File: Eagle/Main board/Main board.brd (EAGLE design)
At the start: 160 x 160 mm, 140 parts, among them IC1 LMZ14202TZE-ADJ_NOPB, IC2 VNH7070ASTR, IC3 VNH7070ASTR, IC4 VNH7070ASTR, IC5 VNH7070ASTR, IC6 ATMEGA32U4-AU, J2 43650-0201, J3 43650-0201, J4 43650-0201, J5 43650-0201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

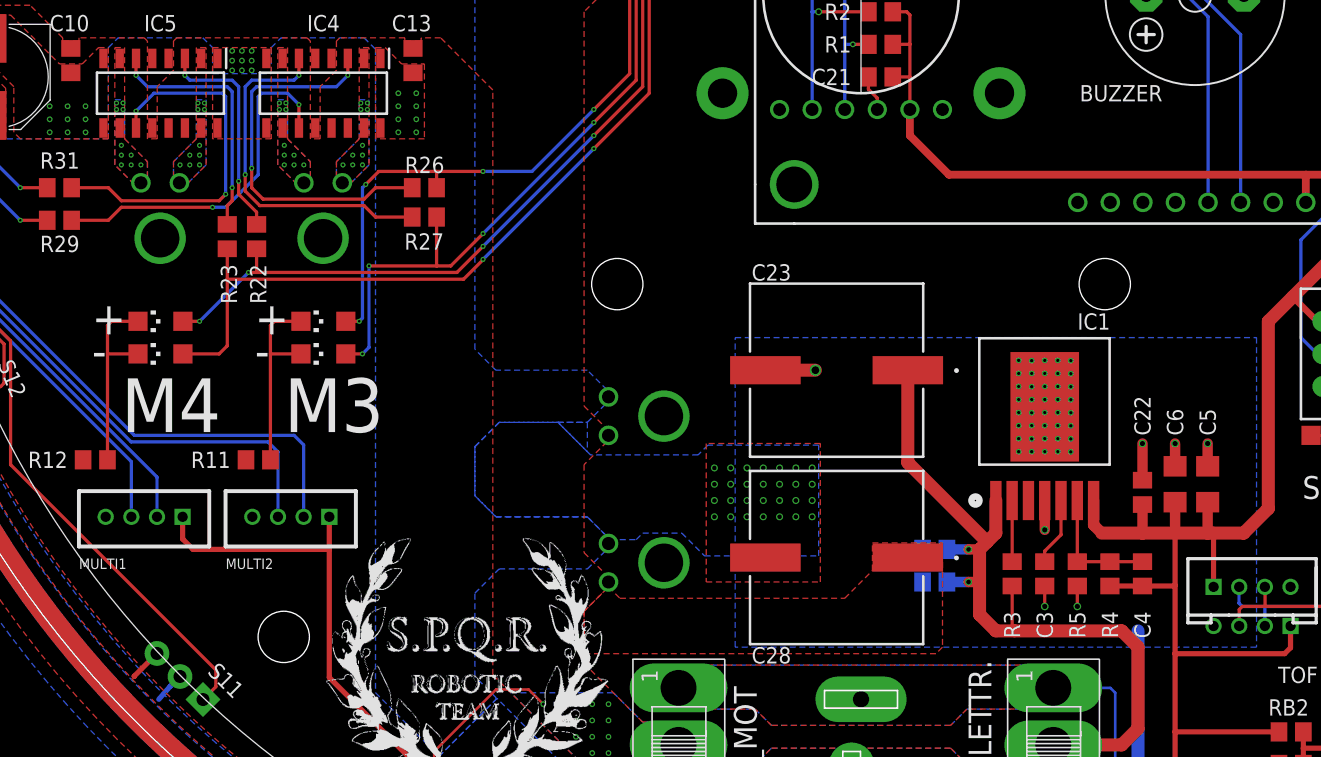
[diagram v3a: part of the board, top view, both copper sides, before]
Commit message: Added JLC's order number place, cleaned files
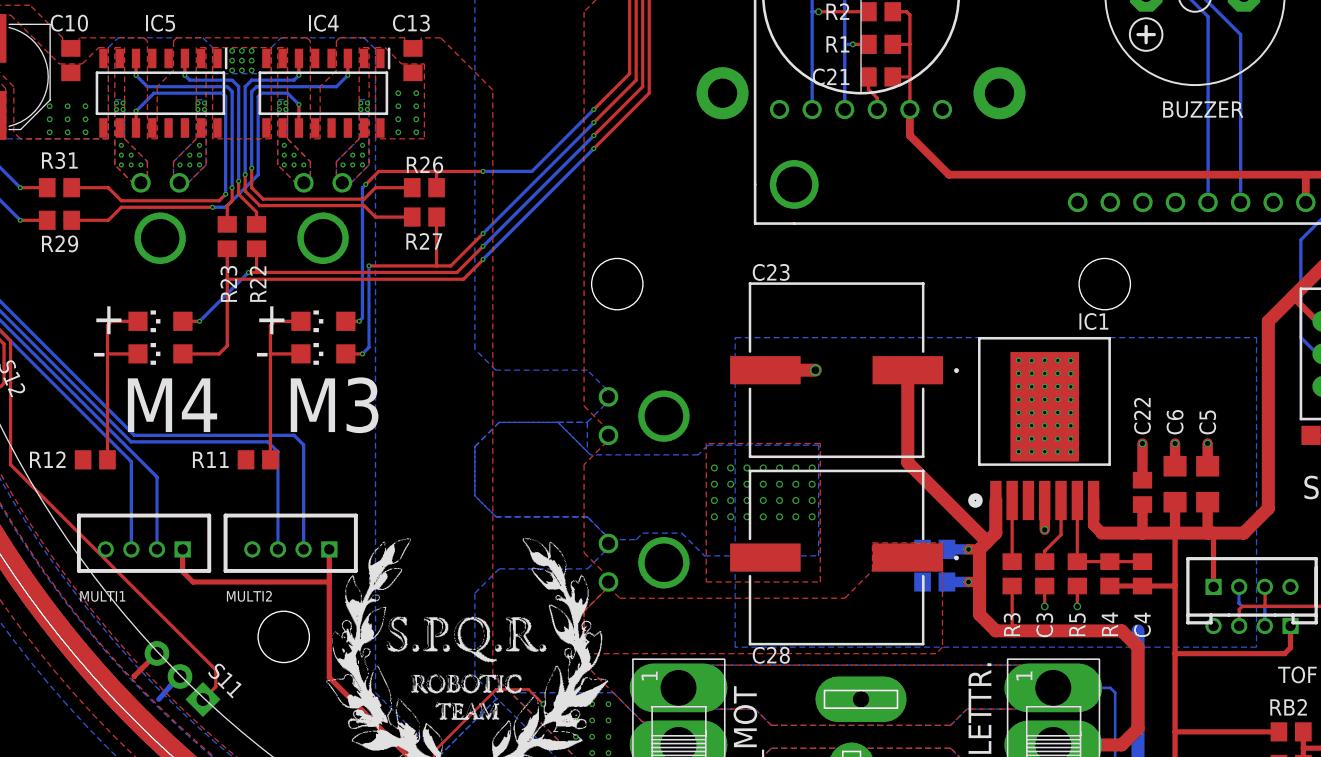
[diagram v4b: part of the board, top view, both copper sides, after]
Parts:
- moved MULTI1 2.54 mm to (-44.5, -43.2)
- moved MULTI2 2.54 mm to (-55.9, -43.2)
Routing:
- net +3V3: track 636.0 -> 633.5 mm
- net MULTI_DIG2: track 180.8 -> 183.4 mm
- net MULTI_DIG1: track 183.8 -> 186.3 mm
- net MULTI_PWM2: track 177.4 -> 179.9 mm
- net MULTI_PWM1: track 181.3 -> 183.9 mm
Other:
- board text added: "JLCJLCJLCJLC"
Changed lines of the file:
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@@
 <layer number="19" name="Unrouted" color="6" fill="1" visible="yes" active="yes"/>
 <layer number="20" name="Dimension" color="24" fill="1" visible="yes" active="yes"/>
-<layer number="21" name="tPlace" color="7" fill="1" visible="yes" active="yes"/>
+<layer number="21" name="tPlace" color="7" fill="1" visible="no" active="yes"/>
 <layer number="22" name="bPlace" color="7" fill="1" visible="yes" active="yes"/>
-<layer number="23" name="tOrigins" color="15" fill="1" visible="yes" active="yes"/>
+<layer number="23" name="tOrigins" color="15" fill="1" visible="no" active="yes"/>
 <layer number="24" name="bOrigins" color="15" fill="1" visible="yes" active="yes"/>
 <layer number="25" name="tNames" color="7" fill="1" visible="yes" active="yes"/>
@@
 <layer number="37" name="tTest" color="7" fill="1" visible="no" active="yes"/>
 <layer number="38" name="bTest" color="7" fill="1" visible="no" active="yes"/>
-<layer number="39" name="tKeepout" color="4" fill="11" visible="yes" active="yes"/>
+<layer number="39" name="tKeepout" color="4" fill="11" visible="no" active="yes"/>
 <layer number="40" name="bKeepout" color="1" fill="11" visible="yes" active="yes"/>
-<layer number="41" name="tRestrict" color="4" fill="10" visible="yes" active="yes"/>
+<layer number="41" name="tRestrict" color="4" fill="10" visible="no" active="yes"/>
 <layer number="42" name="bRestrict" color="1" fill="10" visible="yes" active="yes"/>
 <layer number="43" name="vRestrict" color="2" fill="10" visible="no" active="yes"/>
@@
 <layer number="49" name="Reference" color="7" fill="1" visible="no" active="yes"/>
 <layer number="50" name="dxf" color="7" fill="1" visible="no" active="no"/>
-<layer number="51" name="tDocu" color="7" fill="1" visible="yes" active="yes"/>
+<layer number="51" name="tDocu" color="7" fill="1" visible="no" active="yes"/>
 <layer number="52" name="bDocu" color="7" fill="1" visible="yes" active="yes"/>
 <layer number="53" name="tGND_GNDA" color="7" fill="1" visible="no" active="no"/>
@@
 <text x="49.53" y="23.368" size="0.8128" layer="25">PALLA_PRESA</text>
 <text x="56.642" y="23.368" size="0.8128" layer="26" rot="MR0">PALLA_PRESA</text>
-<wire x1="-60.966" y1="-38.636" x2="-50.806" y2="-38.636" width="0.3048" layer="25"/>
-<wire x1="-50.806" y1="-38.636" x2="-50.806" y2="-42.954" width="0.3048" layer="25"/>
-<wire x1="-50.806" y1="-42.954" x2="-60.966" y2="-42.954" width="0.3048" layer="25"/>
-<wire x1="-60.966" y1="-42.954" x2="-60.966" y2="-38.636" width="0.3048" layer="25"/>
-<wire x1="-49.536" y1="-38.636" x2="-39.376" y2="-38.636" width="0.3048" layer="25"/>
-<wire x1="-39.376" y1="-38.636" x2="-39.376" y2="-42.954" width="0.3048" layer="25"/>
-<wire x1="-39.376" y1="-42.954" x2="-49.536" y2="-42.954" width="0.3048" layer="25"/>
-<wire x1="-49.536" y1="-42.954" x2="-49.536" y2="-38.636" width="0.3048" layer="25"/>
-<text x="-60.96" y="-44.704" size="0.8128" layer="25">MULTI1</text>
-<text x="-49.53" y="-44.704" size="0.8128" layer="25">MULTI2</text>
+<wire x1="-60.966" y1="-40.541" x2="-50.806" y2="-40.541" width="0.3048" layer="25"/>
+<wire x1="-50.806" y1="-40.541" x2="-50.806" y2="-44.859" width="0.3048" layer="25"/>
+<wire x1="-50.806" y1="-44.859" x2="-60.966" y2="-44.859" width="0.3048" layer="25"/>
+<wire x1="-60.966" y1="-44.859" x2="-60.966" y2="-40.541" width="0.3048" layer="25"/>
+<wire x1="-49.536" y1="-40.541" x2="-39.376" y2="-40.541" width="0.3048" layer="25"/>
+<wire x1="-39.376" y1="-40.541" x2="-39.376" y2="-44.859" width="0.3048" layer="25"/>
+<wire x1="-39.376" y1="-44.859" x2="-49.536" y2="-44.859" width="0.3048" layer="25"/>
+<wire x1="-49.536" y1="-44.859" x2="-49.536" y2="-40.541" width="0.3048" layer="25"/>
+<text x="-60.96" y="-47.244" size="0.8128" layer="25">MULTI1</text>
+<text x="-49.53" y="-47.244" size="0.8128" layer="25">MULTI2</text>
 <rectangle x1="-28.014290625" y1="-61.546103125" x2="-27.719653125" y2="-61.509271875" layer="25"/>
 <rectangle x1="-28.1616125" y1="-61.509271875" x2="-27.682825" y2="-61.472446875" layer="25"/>
@@
 <text x="-33.02" y="31.115" size="1.778" layer="26" rot="MR0">Morco</text>
 <text x="5.08" y="43.18" size="1.27" layer="26" rot="MR0">Designed by Dario Casagrande</text>
+<text x="5.08" y="5.715" size="1.016" layer="26" rot="MR0">JLCJLCJLCJLC</text>
 </plain>
 <attributes>
@@
 <attribute name="MF" value="" x="1.905" y="72.39" size="1.778" layer="27" rot="R180" display="off"/>
 <attribute name="MPN" value="" x="1.905" y="72.39" size="1.778" layer="27" rot="R180" display="off"/>
-<attribute name="NAME" x="23.495" y="-6.985" size="1.27" layer="25" ratio="10" rot="R180"/>
+<attribute name="NAME" x="29.845" y="-8.255" size="1.27" layer="25" ratio="10" rot="R180"/>
 <attribute name="OC_FARNELL" value="unknown" x="1.905" y="72.39" size="1.778" layer="27" rot="R180" display="off"/>
 <attribute name="OC_NEWARK" value="unknown" x="1.905" y="72.39" size="1.778" layer="27" rot="R180" display="off"/>
@@
 <attribute name="VALUE" x="5.715" y="41.275" size="1.27" layer="27" rot="R180"/>
 </element>
-<element name="MULTI1" library="CONNECTER" package="2.0_1X4" value="TWIG_2.0" x="-44.45" y="-40.64" smashed="yes" rot="MR0">
-<attribute name="NAME" x="-39.513" y="-44.409" size="0.8128" layer="26" font="vector" ratio="10" rot="MR0"/>
-<attribute name="NAME" x="-39.65" y="-39.84" size="0.8128" layer="34" font="vector" ratio="10" rot="MR0"/>
-</element>
-<element name="MULTI2" library="CONNECTER" package="2.0_1X4" value="TWIG_2.0" x="-55.88" y="-40.64" smashed="yes" rot="MR0">
-<attribute name="NAME" x="-50.943" y="-44.663" size="0.8128" layer="26" font="vector" ratio="10" rot="MR0"/>
-<attribute name="NAME" x="-51.08" y="-39.84" size="0.8128" layer="34" font="vector" ratio="10" rot="MR0"/>
+<element name="MULTI1" library="CONNECTER" package="2.0_1X4" value="TWIG_2.0" x="-44.45" y="-43.18" smashed="yes" rot="MR0">
+<attribute name="NAME" x="-45.863" y="-46.949" size="0.8128" layer="26" font="vector" ratio="10" rot="MR0"/>
+<attribute name="NAME" x="-39.65" y="-42.38" size="0.8128" layer="34" font="vector" ratio="10" rot="MR0"/>
+</element>
+<element name="MULTI2" library="CONNECTER" package="2.0_1X4" value="TWIG_2.0" x="-55.88" y="-43.18" smashed="yes" rot="MR0">
+<attribute name="NAME" x="-57.293" y="-47.203" size="0.8128" layer="26" font="vector" ratio="10" rot="MR0"/>
+<attribute name="NAME" x="-51.08" y="-42.38" size="0.8128" layer="34" font="vector" ratio="10" rot="MR0"/>
 </element>
 <element name="J2" library="Molex motori" package="43650-0200" value="43650-0201" x="-19.685" y="-34.29" smashed="yes" rot="MR270">
@@
 <contactref element="MULTI1" pad="1"/>
 <contactref element="MULTI2" pad="1"/>
-<wire x1="-52.88" y1="-40.64" x2="-52.88" y2="-42.37" width="0.4064" layer="1"/>
-<wire x1="-52.88" y1="-42.37" x2="-52.07" y2="-43.18" width="0.4064" layer="1"/>
-<wire x1="-41.45" y1="-40.64" x2="-41.45" y2="-43.18" width="0.4064" layer="1"/>
-<wire x1="-41.45" y1="-43.18" x2="-41.45" y2="-53.165" width="0.4064" layer="1"/>
+<wire x1="-52.88" y1="-43.18" x2="-52.88" y2="-44.91" width="0.4064" layer="1"/>
+<wire x1="-52.88" y1="-44.91" x2="-52.07" y2="-45.72" width="0.4064" layer="1"/>
+<wire x1="-41.45" y1="-43.18" x2="-41.45" y2="-45.72" width="0.4064" layer="1"/>
+<wire x1="-41.45" y1="-45.72" x2="-41.45" y2="-53.165" width="0.4064" layer="1"/>
 <wire x1="-41.45" y1="-53.165" x2="-34.29" y2="-60.325" width="0.4064" layer="1"/>
-<wire x1="-52.07" y1="-43.18" x2="-41.45" y2="-43.18" width="0.4064" layer="1"/>
+<wire x1="-52.07" y1="-45.72" x2="-41.45" y2="-45.72" width="0.4064" layer="1"/>
 <wire x1="-34.61" y1="-62.23" x2="-34.61" y2="-60.645" width="0.4064" layer="1"/>
 <wire x1="-34.61" y1="-60.645" x2="-34.29" y2="-60.325" width="0.4064" layer="1"/>
@@
 <wire x1="-70.104" y1="16.764" x2="-70.104" y2="-20.828" width="0.254" layer="16"/>
 <wire x1="-56.642" y1="-34.29" x2="-70.104" y2="-20.828" width="0.254" layer="16"/>
-<wire x1="-43.45" y1="-40.64" x2="-43.45" y2="-35.036" width="0.254" layer="16"/>
+<wire x1="-43.45" y1="-43.18" x2="-43.45" y2="-35.036" width="0.254" layer="16"/>
 <wire x1="-43.45" y1="-35.036" x2="-44.196" y2="-34.29" width="0.254" layer="16"/>
 <wire x1="-44.196" y1="-34.29" x2="-56.642" y2="-34.29" width="0.254" layer="16"/>
@@
 <wire x1="-70.612" y1="17.018" x2="-70.612" y2="-21.082" width="0.254" layer="16"/>
 <wire x1="-70.612" y1="-21.082" x2="-56.896" y2="-34.798" width="0.254" layer="16"/>
-<wire x1="-45.45" y1="-35.576" x2="-45.45" y2="-40.64" width="0.254" layer="16"/>
+<wire x1="-45.45" y1="-35.576" x2="-45.45" y2="-43.18" width="0.254" layer="16"/>
 <wire x1="-56.896" y1="-34.798" x2="-46.228" y2="-34.798" width="0.254" layer="16"/>
 <wire x1="-46.228" y1="-34.798" x2="-45.45" y2="-35.576" width="0.254" layer="16"/>
@@
 <wire x1="-71.12" y1="17.272" x2="-71.12" y2="-21.304" width="0.254" layer="16"/>
 <wire x1="-71.12" y1="-21.304" x2="-54.88" y2="-37.544" width="0.254" layer="16"/>
-<wire x1="-54.88" y1="-37.544" x2="-54.88" y2="-40.64" width="0.254" layer="16"/>
+<wire x1="-54.88" y1="-37.544" x2="-54.88" y2="-43.18" width="0.254" layer="16"/>
 </signal>
 <signal name="MULTI_DIG2">
@@
 <wire x1="-71.628" y1="17.526" x2="-71.628" y2="-21.59" width="0.254" layer="16"/>
 <wire x1="-71.628" y1="-21.59" x2="-56.88" y2="-36.338" width="0.254" layer="16"/>
-<wire x1="-56.88" y1="-36.338" x2="-56.88" y2="-40.64" width="0.254" layer="16"/>
+<wire x1="-56.88" y1="-36.338" x2="-56.88" y2="-43.18" width="0.254" layer="16"/>
 </signal>
 <signal name="N$24">

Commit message: Final commit
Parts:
- renumbered ELECT to LD_ELECT
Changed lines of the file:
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@@
 <drawing>
 <settings>
-<setting alwaysvectorfont="yes"/>
+<setting alwaysvectorfont="no"/>
 <setting verticaltext="up"/>
 </settings>
@@
 <layer number="19" name="Unrouted" color="6" fill="1" visible="yes" active="yes"/>
 <layer number="20" name="Dimension" color="24" fill="1" visible="yes" active="yes"/>
-<layer number="21" name="tPlace" color="7" fill="1" visible="no" active="yes"/>
+<layer number="21" name="tPlace" color="7" fill="1" visible="yes" active="yes"/>
 <layer number="22" name="bPlace" color="7" fill="1" visible="yes" active="yes"/>
-<layer number="23" name="tOrigins" color="15" fill="1" visible="no" active="yes"/>
+<layer number="23" name="tOrigins" color="15" fill="1" visible="yes" active="yes"/>
 <layer number="24" name="bOrigins" color="15" fill="1" visible="yes" active="yes"/>
 <layer number="25" name="tNames" color="7" fill="1" visible="yes" active="yes"/>
@@
 <layer number="37" name="tTest" color="7" fill="1" visible="no" active="yes"/>
 <layer number="38" name="bTest" color="7" fill="1" visible="no" active="yes"/>
-<layer number="39" name="tKeepout" color="4" fill="11" visible="no" active="yes"/>
+<layer number="39" name="tKeepout" color="4" fill="11" visible="yes" active="yes"/>
 <layer number="40" name="bKeepout" color="1" fill="11" visible="yes" active="yes"/>
-<layer number="41" name="tRestrict" color="4" fill="10" visible="no" active="yes"/>
+<layer number="41" name="tRestrict" color="4" fill="10" visible="yes" active="yes"/>
 <layer number="42" name="bRestrict" color="1" fill="10" visible="yes" active="yes"/>
 <layer number="43" name="vRestrict" color="2" fill="10" visible="no" active="yes"/>
@@
 <layer number="49" name="Reference" color="7" fill="1" visible="no" active="yes"/>
 <layer number="50" name="dxf" color="7" fill="1" visible="no" active="no"/>
-<layer number="51" name="tDocu" color="7" fill="1" visible="no" active="yes"/>
+<layer number="51" name="tDocu" color="7" fill="1" visible="yes" active="yes"/>
 <layer number="52" name="bDocu" color="7" fill="1" visible="yes" active="yes"/>
 <layer number="53" name="tGND_GNDA" color="7" fill="1" visible="no" active="no"/>
@@
 <attribute name="VALUE" x="-14.859" y="-66.548" size="1.27" layer="28" rot="MR180"/>
 </element>
-<element name="ELECT" library="led" library_urn="urn:adsk.eagle:library:259" package="CHIPLED_1206" package3d_urn="urn:adsk.eagle:package:15823/2" value="" x="14.986" y="-69.088" smashed="yes" rot="R270">
+<element name="LD_ELECT" library="led" library_urn="urn:adsk.eagle:library:259" package="CHIPLED_1206" package3d_urn="urn:adsk.eagle:package:15823/2" value="" x="14.986" y="-69.088" smashed="yes" rot="R270">
 <attribute name="NAME" x="17.78" y="-70.485" size="1.27" layer="25" rot="R180"/>
 <attribute name="POPULARITY" value="28" x="14.986" y="-69.088" size="1.778" layer="27" rot="R270" display="off"/>
@@
 <wire x1="-34.61" y1="-64.77" x2="-32.766" y2="-64.77" width="0.4064" layer="1"/>
 <contactref element="BAT" pad="C"/>
-<contactref element="ELECT" pad="C"/>
+<contactref element="LD_ELECT" pad="C"/>
 <contactref element="MOT" pad="C"/>
 <contactref element="BALL" pad="4"/>
@@
 <vertex x="-34.29" y="3.302"/>
 <vertex x="-19.05" y="3.302"/>
-<vertex x="-19.05" y="1.27"/>
-<vertex x="-21.59" y="-1.27"/>
+<vertex x="-19.05" y="1.524"/>
+<vertex x="-21.59" y="-1.016"/>
 <vertex x="-21.59" y="-32.004"/>
 <vertex x="-19.812" y="-33.782"/>
@@
 <signal name="N$26">
 <contactref element="R35" pad="1"/>
-<contactref element="ELECT" pad="A"/>
+<contactref element="LD_ELECT" pad="A"/>
 <wire x1="14.036" y1="-69.088" x2="11.938" y2="-69.088" width="0.2032" layer="16"/>
 <via x="11.938" y="-69.088" extent="1-16" drill="0.2"/>
